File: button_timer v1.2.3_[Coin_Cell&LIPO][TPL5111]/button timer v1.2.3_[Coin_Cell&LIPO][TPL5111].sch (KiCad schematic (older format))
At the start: 29 parts, among them J1 Conn_01x05_Female, Q1 mmbt222, SW1 SW_Push, SW2 SW_Push, U1 TPS61097A, U2 AP2112K-3.3, U3 TPL5111, X1 ESP-12E

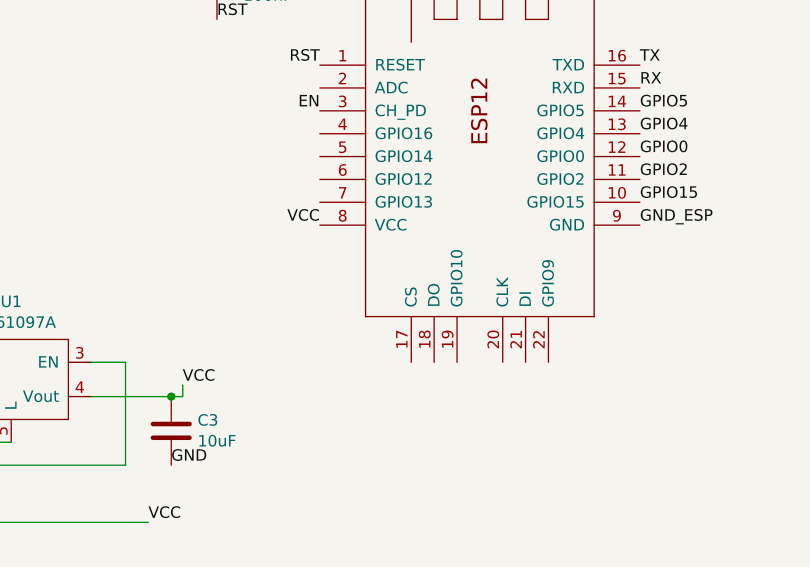
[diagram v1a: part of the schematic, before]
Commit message: cap between esp vcc and ground added
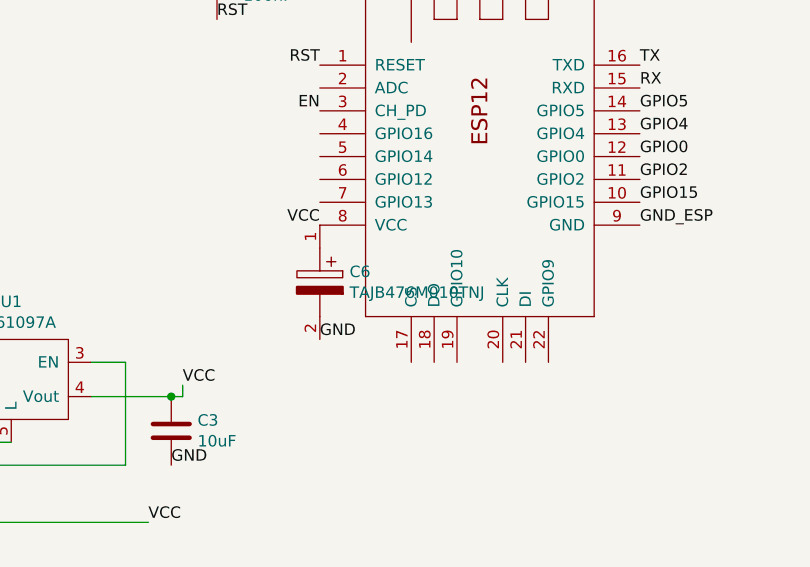
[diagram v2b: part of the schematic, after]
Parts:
- added C6: TAJB476M010TNJ, CAPPM3528X210N, symbol SamacSys_Parts:TAJB476M010TNJ
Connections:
- net GND: now also C6.2
- net VCC: now also C6.1
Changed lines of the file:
@@
 $EndDescr
-$Comp
-L button-timer-v1.2.3_[Coin_Cell&LIPO][TPL5111]-rescue:ESP-12E-ardafruit-button-timer-rescue-button-timer-v1.2-rescue-button-timer-v1.2-rescue-button-timer-v1.2-rescue-button-timer-v1.2-rescue-button-timer-v1.2-rescue X1
-U 1 1 602C0443
-P 6000 3400
-F 0 "X1" H 6000 3400 50  0001 C CNN
-F 1 "ESP-12E" H 6000 3400 50  0001 C CNN
-F 2 "handsolder:ESP-12Elesssilk" H 6000 3400 50  0001 C CNN
-F 3 "" H 6000 3400 50  0001 C CNN
-	1    6000 3400
-	1    0    0    -1
-$EndComp
 $Comp
 L button-timer-v1.2.3_[Coin_Cell&LIPO][TPL5111]-rescue:Battery_Cell-Device-button-timer-rescue-button-timer-v1.2-rescue-button-timer-v1.2-rescue-button-timer-v1.2-rescue-button-timer-v1.2-rescue-button-timer-v1.2-rescue BT1
@@
 	0    1    1    0
 $EndComp
+$Comp
+L SamacSys_Parts:TAJB476M010TNJ C6
+U 1 1 60364975
+P 5300 3700
+F 0 "C6" V 5504 3830 50  0000 L CNN
+F 1 "TAJB476M010TNJ" V 5595 3830 50  0000 L CNN
+F 2 "CAPPM3528X210N" H 5650 3750 50  0001 L CNN
+F 3 "http://datasheets.avx.com/TAJ.pdf" H 5650 3650 50  0001 L CNN
+F 4 "Tantalum Capacitors - Solid SMD 10volts 47uF 20%" H 5650 3550 50  0001 L CNN "Description"
+F 5 "2.1" H 5650 3450 50  0001 L CNN "Height"
+F 6 "AVX" H 5650 3350 50  0001 L CNN "Manufacturer_Name"
+F 7 "TAJB476M010TNJ" H 5650 3250 50  0001 L CNN "Manufacturer_Part_Number"
+F 8 "581-TAJB476M010TNJ" H 5650 3150 50  0001 L CNN "Mouser Part Number"
+F 9 "https://www.mouser.co.uk/ProductDetail/AVX/TAJB476M010TNJ?qs=pYVYkI7xuRVorIKKgcxm0A%3D%3D" H 5650 3050 50  0001 L CNN "Mouser Price/Stock"
+F 10 "TAJB476M010TNJ" H 5650 2950 50  0001 L CNN "Arrow Part Number"
+F 11 "https://www.arrow.com/en/products/tajb476m010tnj/avx" H 5650 2850 50  0001 L CNN "Arrow Price/Stock"
+	1    5300 3700
+	0    1    1    0
+$EndComp
+$Comp
+L button-timer-v1.2.3_[Coin_Cell&LIPO][TPL5111]-rescue:ESP-12E-ardafruit-button-timer-rescue-button-timer-v1.2-rescue-button-timer-v1.2-rescue-button-timer-v1.2-rescue-button-timer-v1.2-rescue-button-timer-v1.2-rescue X1
+U 1 1 602C0443
+P 6000 3400
+F 0 "X1" H 6000 3400 50  0001 C CNN
+F 1 "ESP-12E" H 6000 3400 50  0001 C CNN
+F 2 "handsolder:ESP-12Elesssilk" H 6000 3400 50  0001 C CNN
+F 3 "" H 6000 3400 50  0001 C CNN
+	1    6000 3400
+	1    0    0    -1
+$EndComp
+Text Label 5300 4200 0    50   ~ 0
+GND
 $EndSCHEMATC

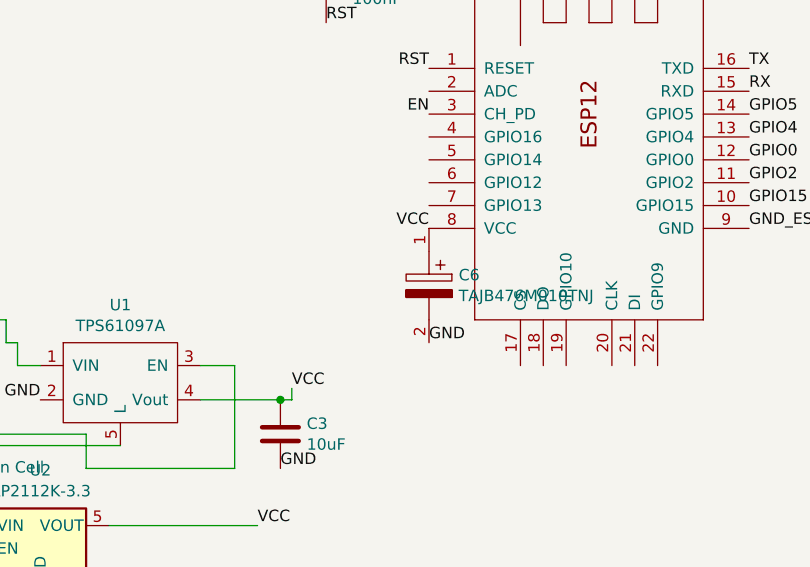
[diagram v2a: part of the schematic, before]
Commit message: Added 100nF decoupling capacitors between VCC and Ground of the ESP
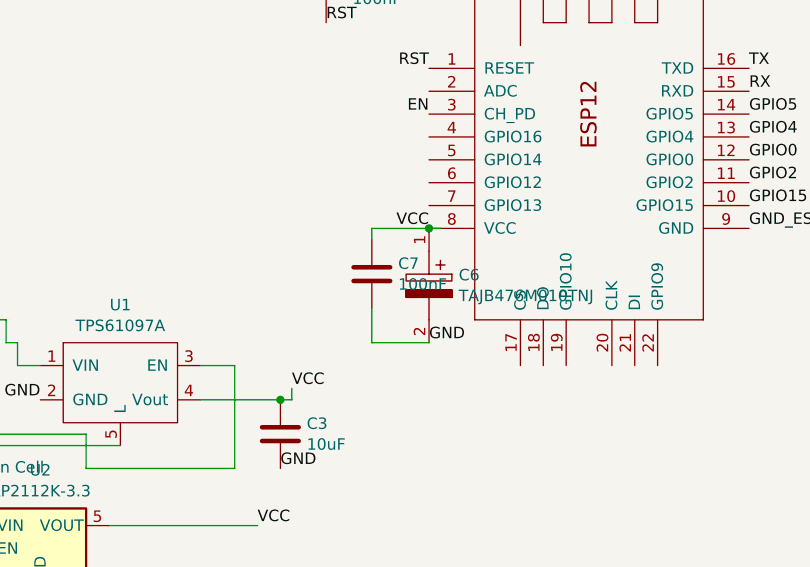
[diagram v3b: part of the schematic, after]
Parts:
- added C7: 100nF, handsolder:C_0402_1005Metric_Pad0.74x0.62mm_HandSoldermod, symbol Device:C
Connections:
- net GND: now also C7.2
- net VCC: now also C7.1
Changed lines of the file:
@@
 Text Label 5300 4200 0    50   ~ 0
 GND
+$Comp
+L Device:C C7
+U 1 1 60368848
+P 5050 3900
+F 0 "C7" H 5165 3946 50  0000 L CNN
+F 1 "100nF" H 5165 3855 50  0000 L CNN
+F 2 "handsolder:C_0402_1005Metric_Pad0.74x0.62mm_HandSoldermod" H 5088 3750 50  0001 C CNN
+F 3 "~" H 5050 3900 50  0001 C CNN
+	1    5050 3900
+	1    0    0    -1
+$EndComp
+Wire Wire Line
+	5050 3750 5050 3700
+Wire Wire Line
+	5050 3700 5300 3700
+Connection ~ 5300 3700
+Wire Wire Line
+	5300 3700 5350 3700
+Wire Wire Line
+	5050 4050 5050 4200
+Wire Wire Line
+	5050 4200 5300 4200
 $EndSCHEMATC
